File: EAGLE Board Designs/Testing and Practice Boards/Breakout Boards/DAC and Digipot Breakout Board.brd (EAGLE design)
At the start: 78.6 x 54.7 mm, 34 parts, among them J1 JUMPER.1, X1 CONNECTOR-4NANO-FIT-VERTICAL-4

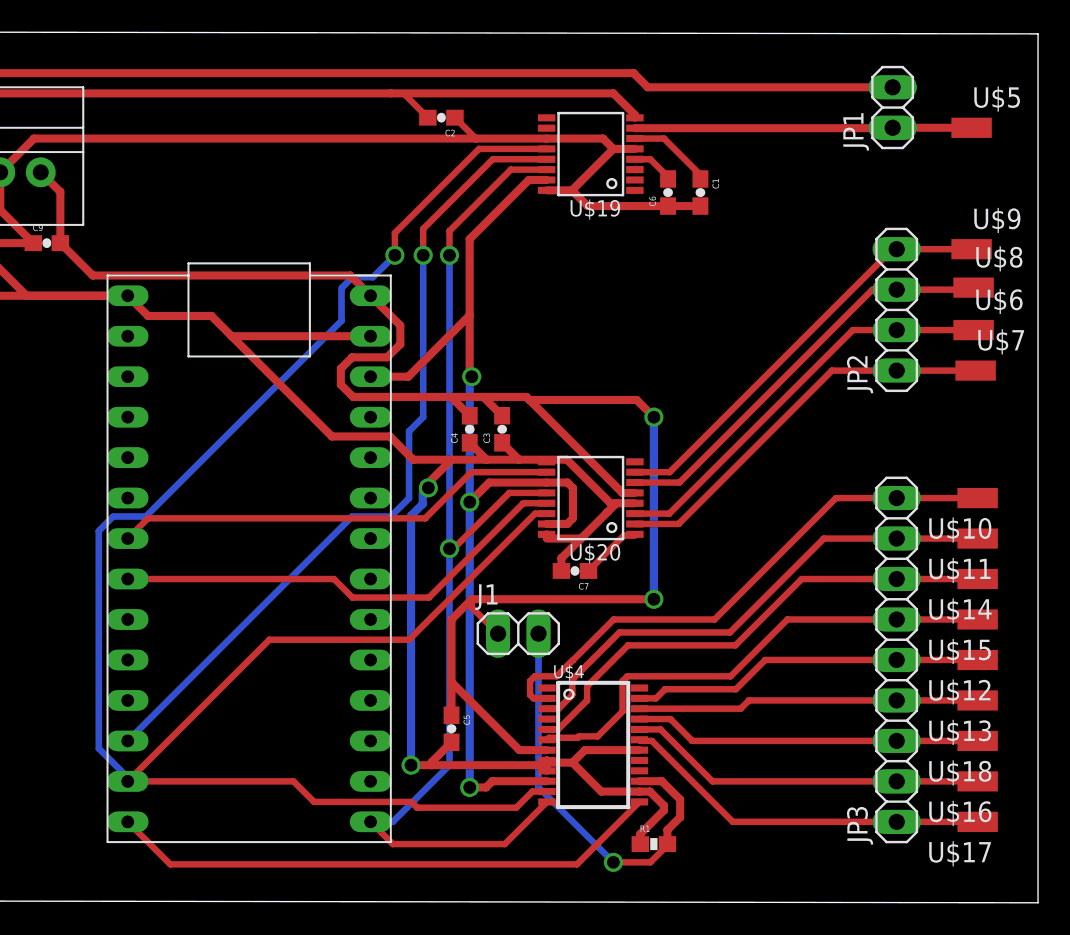
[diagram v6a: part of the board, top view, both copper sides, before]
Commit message: add pad for ground
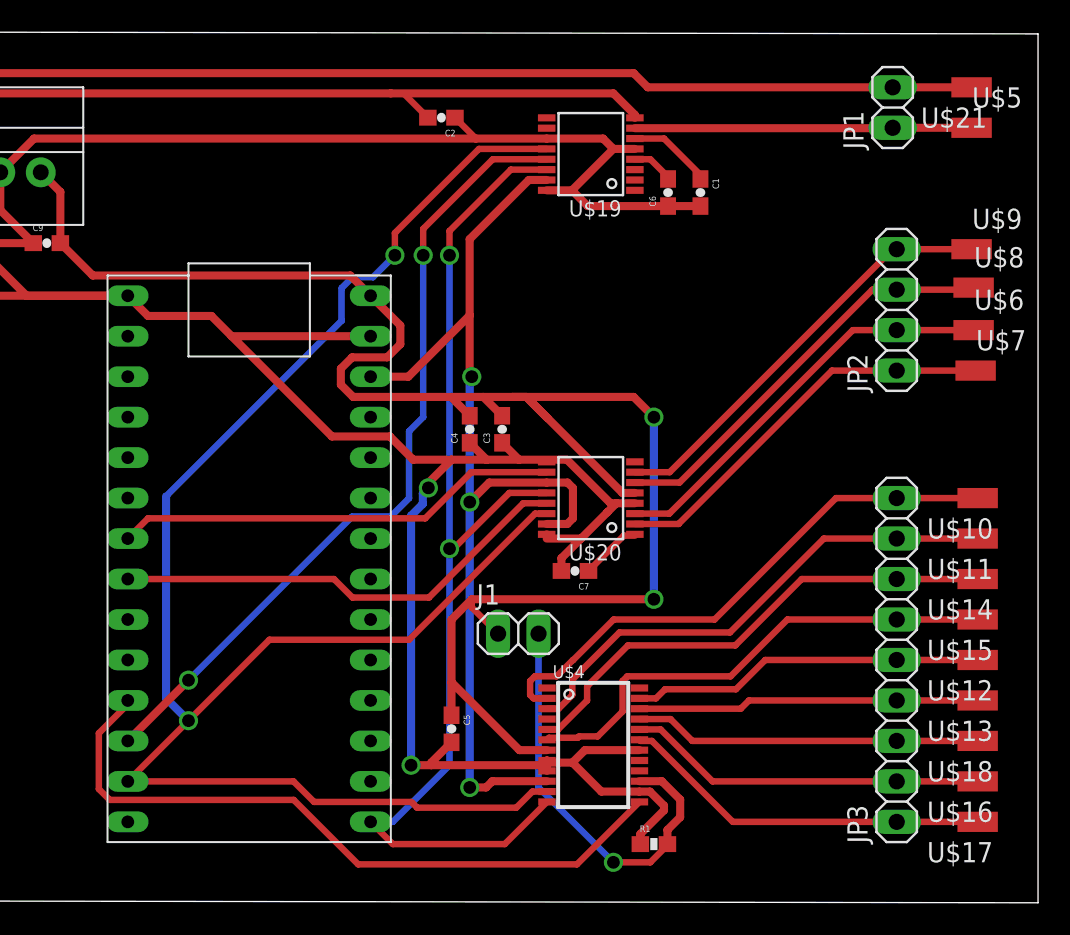
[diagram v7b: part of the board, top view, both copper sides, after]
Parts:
- added U$21: SOLDER_PAD, HyTechDevices:SOLDER_PAD_XSMALL
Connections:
- net CS_3: now also U$2.D9(RX2); no longer U$2.D12
- net GND: now also U$21.P$1
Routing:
- net CS_3: track 34.8 -> 43.8 mm
- net MOSI: track 117.2 -> 110.3 mm, vias 1 -> 2
- net GND: track 279.2 -> 284.2 mm
- net +5V: track 109.1 -> 111.9 mm
- net POTEN_A1: track 35.4 -> 34.9 mm
- net CS_1: vias 1 -> 2
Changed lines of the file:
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@@
 <attribute name="VALUE" x="29.337" y="53.975" size="0.8128" layer="27" align="top-left"/>
+</element>
+<element name="U$21" library="HyTechDevices" package="SOLDER_PAD_XSMALL" value="SOLDER_PAD" x="55.499" y="99.441" smashed="yes">
+<attribute name="NAME" x="52.324" y="96.901" size="1.27" layer="25"/>
 </element>
 </elements>
@@
 <wire x1="16.6808375" y1="80.01" x2="22.86" y2="80.01" width="0.508" layer="1"/>
 <wire x1="22.86" y1="80.01" x2="24.853" y2="80.01" width="0.508" layer="1"/>
-<wire x1="24.853" y1="80.01" x2="27.559" y2="80.01" width="0.508" layer="1"/>
+<wire x1="24.853" y1="80.01" x2="26.67" y2="80.01" width="0.508" layer="1"/>
+<wire x1="26.67" y1="80.01" x2="27.559" y2="80.01" width="0.508" layer="1"/>
 <wire x1="34.3678" y1="73.985" x2="33.584" y2="73.985" width="0.508" layer="1"/>
 <wire x1="33.584" y1="73.985" x2="27.7495" y2="79.8195" width="0.508" layer="1"/>
@@
 <wire x1="0.342" y1="87.63" x2="-1.69" y2="89.662" width="0.508" layer="1"/>
 <contactref element="U$4" pad="7"/>
-<wire x1="27.7495" y1="79.8195" x2="34.4805" y2="79.8195" width="0.508" layer="1"/>
-<wire x1="34.4805" y1="79.8195" x2="35.56" y2="78.74" width="0.508" layer="1"/>
+<wire x1="27.7495" y1="79.8195" x2="28.8925" y2="78.6765" width="0.508" layer="1"/>
 <via x="35.56" y="78.74" extent="1-16" drill="0.8"/>
 <wire x1="35.56" y1="78.74" x2="35.56" y2="67.31" width="0.508" layer="16"/>
@@
 <wire x1="24.13" y1="67.31" x2="24.13" y2="66.802" width="0.4064" layer="1"/>
 <wire x1="24.13" y1="66.802" x2="25.781" y2="65.151" width="0.4064" layer="1"/>
+<wire x1="35.56" y1="78.74" x2="34.29" y2="80.01" width="0.508" layer="1"/>
+<wire x1="34.29" y1="80.01" x2="26.67" y2="80.01" width="0.508" layer="1"/>
 </signal>
 <signal name="GND">
@@
 <wire x1="34.29" y1="100.33" x2="35.179" y2="99.441" width="0.508" layer="1"/>
 <wire x1="35.179" y1="99.441" x2="50.546" y2="99.441" width="0.508" layer="1"/>
+<contactref element="U$21" pad="P$1"/>
+<wire x1="50.546" y1="99.441" x2="55.499" y2="99.441" width="0.508" layer="1"/>
 <wire x1="38.481" y1="91.987" x2="36.449" y2="91.987" width="0" layer="19" extent="1-1"/>
 <wire x1="28.9592" y1="71.258" x2="28.8322" y2="71.1206" width="0" layer="19" extent="1-1"/>
@@
 <wire x1="16.64468125" y1="87.522" x2="17.926" y2="87.522" width="0.4064" layer="16"/>
 <wire x1="17.926" y1="87.522" x2="19.304" y2="88.9" width="0.4064" layer="16"/>
-<wire x1="2.54" y1="55.88" x2="2.54" y2="56.12268125" width="0.4064" layer="16"/>
-<wire x1="2.54" y1="56.12268125" x2="0.724" y2="57.93868125" width="0.4064" layer="16"/>
-<wire x1="0.724" y1="71.60131875" x2="1.62068125" y2="72.498" width="0.4064" layer="16"/>
-<wire x1="1.62068125" y1="72.498" x2="3.67531875" y2="72.498" width="0.4064" layer="16"/>
-<wire x1="3.67531875" y1="72.498" x2="15.964" y2="84.78668125" width="0.4064" layer="16"/>
+<wire x1="4.94531875" y1="73.768" x2="15.964" y2="84.78668125" width="0.4064" layer="16"/>
 <wire x1="15.964" y1="84.78668125" x2="15.964" y2="86.84131875" width="0.4064" layer="16"/>
-<wire x1="0.724" y1="57.93868125" x2="0.724" y2="71.60131875" width="0.4064" layer="16"/>
 <wire x1="19.304" y1="90.297" x2="19.304" y2="88.9" width="0.4064" layer="1"/>
 <wire x1="28.8322" y1="95.575" x2="24.582" y2="95.575" width="0.4064" layer="1"/>
@@
 <wire x1="28.108" y1="72.685" x2="20.193" y2="64.77" width="0.4064" layer="1"/>
 <wire x1="20.193" y1="64.77" x2="11.43" y2="64.77" width="0.4064" layer="1"/>
-<wire x1="11.43" y1="64.77" x2="2.54" y2="55.88" width="0.4064" layer="1"/>
+<wire x1="11.43" y1="64.77" x2="6.35" y2="59.69" width="0.4064" layer="1"/>
 <contactref element="U$4" pad="11"/>
+<wire x1="6.35" y1="59.69" x2="2.54" y2="55.88" width="0.4064" layer="1"/>
 <wire x1="27.936" y1="55.241" x2="28.85" y2="55.241" width="0.4064" layer="1"/>
 <wire x1="12.94268125" y1="55.88" x2="2.54" y2="55.88" width="0.4064" layer="1"/>
@@
 <wire x1="20.339" y1="54.591" x2="14.23168125" y2="54.591" width="0.4064" layer="1"/>
 <wire x1="14.23168125" y1="54.591" x2="12.94268125" y2="55.88" width="0.4064" layer="1"/>
+<via x="6.35" y="59.69" extent="1-16" drill="0.8"/>
+<wire x1="4.94531875" y1="73.768" x2="4.94531875" y2="61.09468125" width="0.508" layer="16"/>
+<wire x1="4.94531875" y1="61.09468125" x2="6.35" y2="59.69" width="0.508" layer="16"/>
 </signal>
 <signal name="5V_DAC_OUTPUT_A">
@@
 <contactref element="U$20" pad="10"/>
 <contactref element="U$2" pad="D5"/>
-<wire x1="3.81" y1="72.39" x2="2.54" y2="71.12" width="0.4064" layer="1"/>
+<wire x1="2.54" y1="71.12" x2="3.81" y2="72.39" width="0.4064" layer="1"/>
 <wire x1="3.81" y1="72.39" x2="21.209" y2="72.39" width="0.4064" layer="1"/>
 <wire x1="28.8322" y1="75.285" x2="24.104" y2="75.285" width="0.4064" layer="1"/>
@@
 <contactref element="U$10" pad="P$1"/>
 <contactref element="U$4" pad="2"/>
-<wire x1="30.11705625" y1="63.119" x2="30.489028125" y2="63.490971875" width="0.4064" layer="1"/>
 <contactref element="JP3" pad="9"/>
 <wire x1="30.489028125" y1="63.490971875" x2="33.03805625" y2="66.04" width="0.4064" layer="1"/>
@@
 <contactref element="U$19" pad="13"/>
 <via x="21.082" y="88.9" extent="1-16" drill="0.8"/>
-<wire x1="2.54" y1="58.42" x2="16.618" y2="72.498" width="0.4064" layer="16"/>
+<wire x1="6.35" y1="62.23" x2="16.618" y2="72.498" width="0.4064" layer="16"/>
 <wire x1="16.618" y1="72.498" x2="19.04231875" y2="72.498" width="0.4064" layer="16"/>
 <wire x1="19.04231875" y1="72.498" x2="20.193" y2="73.64868125" width="0.4064" layer="16"/>
@@
 <wire x1="28.8322" y1="94.925" x2="25.449525" y2="94.925" width="0.4064" layer="1"/>
 <wire x1="25.449525" y1="94.925" x2="21.082" y2="90.557475" width="0.4064" layer="1"/>
+<wire x1="2.54" y1="58.42" x2="6.35" y2="62.23" width="0.508" layer="1"/>
+<via x="6.35" y="62.23" extent="1-16" drill="0.8"/>
 </signal>
 <signal name="CS_2">
@@
 </signal>
 <signal name="CS_3">
-<contactref element="U$2" pad="D12"/>
 <contactref element="U$4" pad="13"/>
 <wire x1="34.65" y1="54.591" x2="30.732" y2="50.673" width="0.4064" layer="1"/>
-<wire x1="30.732" y1="50.673" x2="5.207" y2="50.673" width="0.4064" layer="1"/>
-<wire x1="5.207" y1="50.673" x2="2.54" y2="53.34" width="0.4064" layer="1"/>
+<contactref element="U$2" pad="D9(RX2)"/>
+<wire x1="30.732" y1="50.673" x2="17.00020625" y2="50.673" width="0.4064" layer="1"/>
+<wire x1="1.40468125" y1="54.718" x2="0.724" y2="55.39868125" width="0.4064" layer="1"/>
+<wire x1="12.95520625" y1="54.718" x2="1.40468125" y2="54.718" width="0.4064" layer="1"/>
+<wire x1="0.724" y1="58.90131875" x2="2.54" y2="60.71731875" width="0.4064" layer="1"/>
+<wire x1="2.54" y1="60.71731875" x2="2.54" y2="60.96" width="0.4064" layer="1"/>
+<wire x1="0.724" y1="55.39868125" x2="0.724" y2="58.90131875" width="0.4064" layer="1"/>
+<wire x1="17.00020625" y1="50.673" x2="12.95520625" y2="54.718" width="0.4064" layer="1"/>
 </signal>
 <signal name="POTEN_B4">

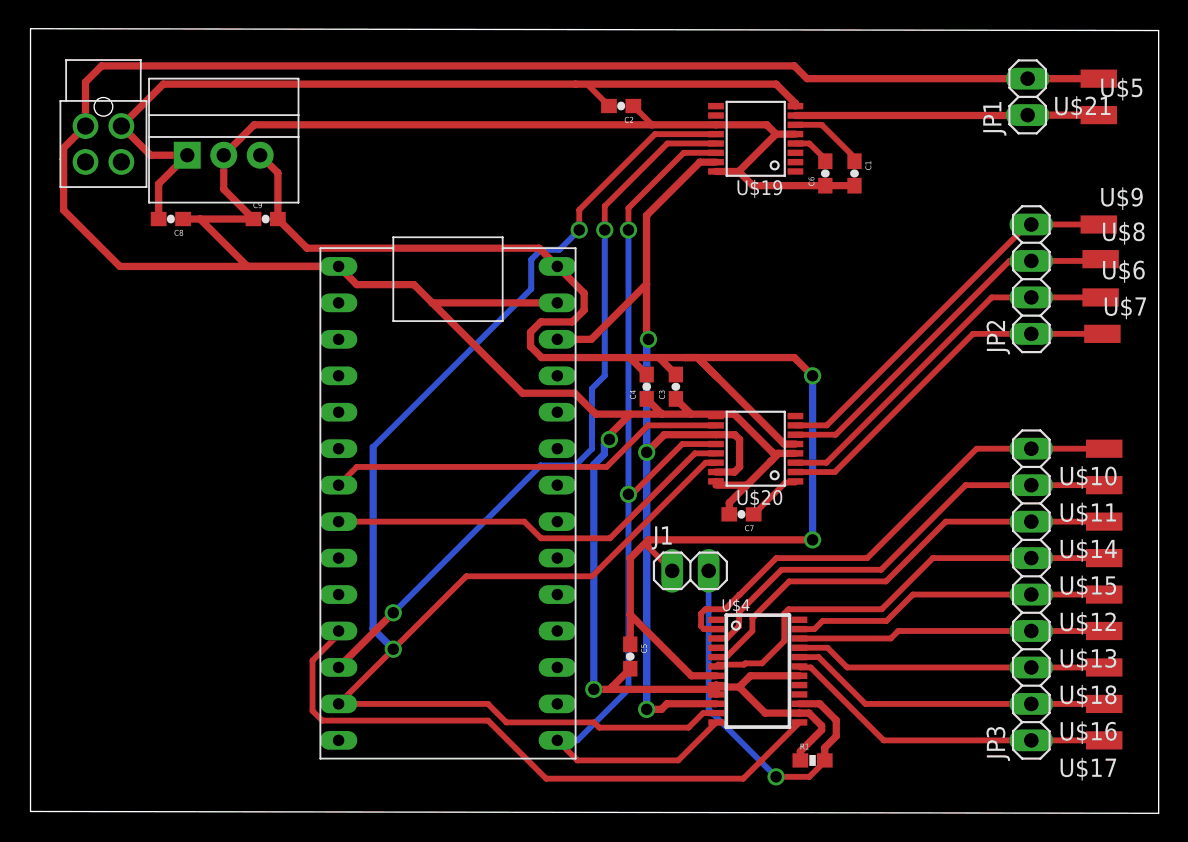
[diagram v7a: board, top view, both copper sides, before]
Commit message: add ratsnest
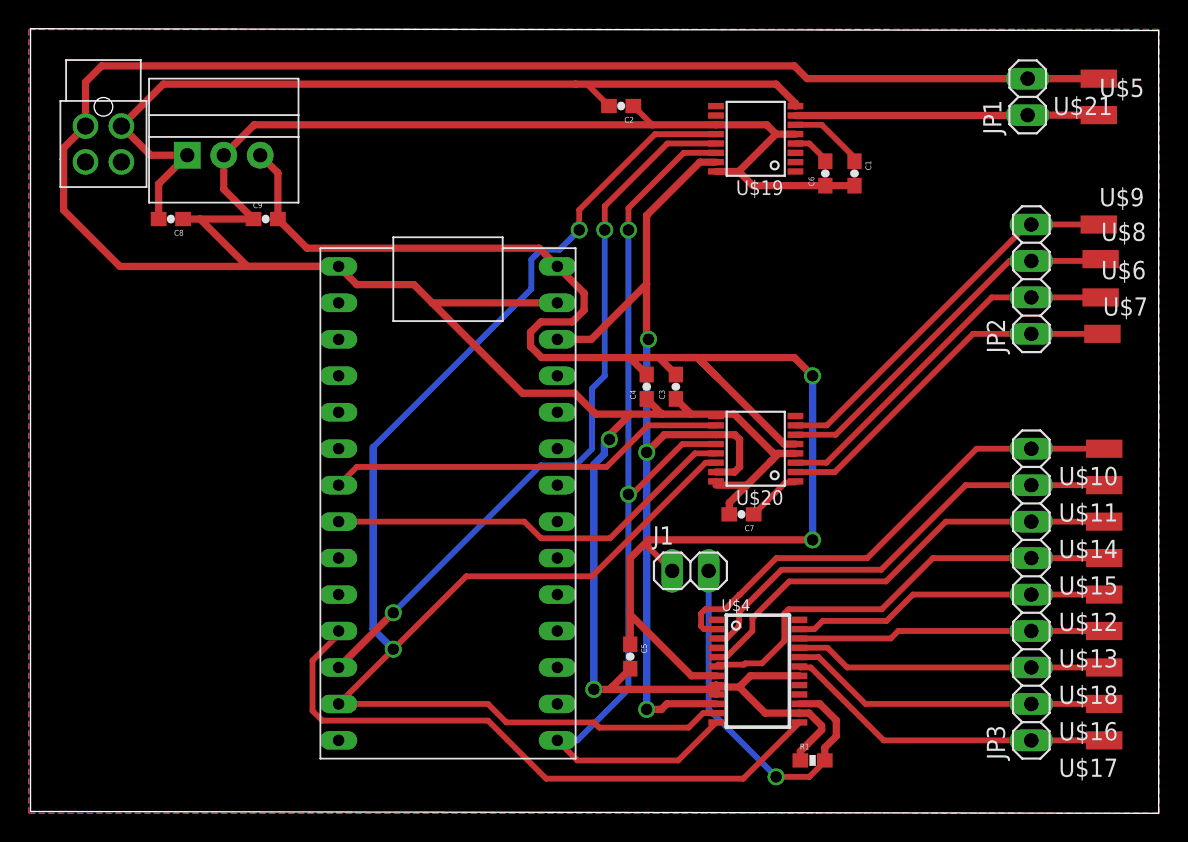
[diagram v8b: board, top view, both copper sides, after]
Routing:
- added copper zone on layer 1, net GND
- added copper zone on layer 16, net GND
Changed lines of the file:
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@@
 <contactref element="U$21" pad="P$1"/>
 <wire x1="50.546" y1="99.441" x2="55.499" y2="99.441" width="0.508" layer="1"/>
-<wire x1="38.481" y1="91.987" x2="36.449" y2="91.987" width="0" layer="19" extent="1-1"/>
-<wire x1="28.9592" y1="71.258" x2="28.8322" y2="71.1206" width="0" layer="19" extent="1-1"/>
-<wire x1="28.8322" y1="75.935" x2="26.035" y2="77.128" width="0" layer="19" extent="1-1"/>
+<polygon width="0.1524" layer="1">
+<vertex x="-19.05" y="102.87"/>
+<vertex x="59.69" y="102.87"/>
+<vertex x="59.69" y="48.26"/>
+<vertex x="-19.05" y="48.26"/>
+</polygon>
+<polygon width="0.1524" layer="16">
+<vertex x="-19.05" y="102.87"/>
+<vertex x="-19.05" y="48.26"/>
+<vertex x="59.69" y="48.26"/>
+<vertex x="59.69" y="102.87"/>
+</polygon>
 </signal>
 <signal name="VSS">
@@
 <wire x1="25.421" y1="55.891" x2="25.029" y2="55.499" width="0.508" layer="1"/>
 <wire x1="25.029" y1="55.499" x2="24.003" y2="55.499" width="0.508" layer="1"/>
-<wire x1="24.003" y1="73.4082" x2="24.003" y2="55.499" width="0" layer="19"/>
-<wire x1="24.003" y1="73.4082" x2="24.003" y2="55.499" width="0" layer="19"/>
 </signal>
 <signal name="12V_DAC_OUTPUT">
@@
 <wire x1="34.3678" y1="72.685" x2="36.5268" y2="72.685" width="0.4064" layer="1"/>
 <wire x1="50.8" y1="84.201" x2="55.626" y2="84.201" width="0.4064" layer="1"/>
-<wire x1="50.8" y1="84.201" x2="55.626" y2="84.201" width="0" layer="19"/>
 </signal>
 <signal name="5V_DAC_OUTPUT_B">
@@
 <wire x1="37.11" y1="72.035" x2="34.3678" y2="72.035" width="0.4064" layer="1"/>
 <wire x1="50.8" y1="81.661" x2="55.753" y2="81.661" width="0.4064" layer="1"/>
-<wire x1="46.736" y1="81.661" x2="55.753" y2="81.661" width="0" layer="19"/>
 </signal>
 <signal name="5V_DAC_OUTPUT_C">
@@
 <wire x1="50.546" y1="89.281" x2="36.55" y2="75.285" width="0.4064" layer="1"/>
 <wire x1="50.8" y1="89.281" x2="55.499" y2="89.281" width="0.4064" layer="1"/>
-<wire x1="50.546" y1="89.281" x2="55.499" y2="89.281" width="0" layer="19"/>
 </signal>
 <signal name="GAIN">
